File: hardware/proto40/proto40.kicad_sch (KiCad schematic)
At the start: 0 parts

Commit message: Generate Proto40 schematic; add generator, project library and CI checks
- hardware/gen: KiCad 10 schematic generator (library import with extends
  flattening, label/power connections on pin ends, multi-instance
  hierarchical sheets, per-instance references, deterministic UUIDs)
- hardware/lib: VDD5 power symbol, TMUX1308 (4051-compatible pinout,
  flagged for datasheet verification)
- hardware/proto40: root, power (USB-C, LM66100, VDD5 shunt clamp,
  3.3 V), MCU (STM32C071, SWD, UART, UI), control (level shifting, STIM
  driver, ADC taps), 2 x side (DIN 41612 C 2x32, 6 groups, 2nd-stage
  mux, 595, bias driver, ID bus), 12 x group8 (channel cells, mux, 165)
- ERC: 0 violations at all severities; netlist design-intent audit passes
- CI: global lib tables, regeneration diff check, Proto40 audit,
  CI_STAGE=schematic skips DRC until layout
- Decision D13 scoped to the ADP-0001 harness only; F9 updated (external
  clamps omitted on Proto40)

Co-Authored-By: Claude Opus 5.5 <noreply@anthropic.com>
Claude-Session: https://claude.ai/code/session_01UG7pR5ZtgvoVGRWFojzQKf
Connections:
- no-connect marks 0 -> 1
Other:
- added sheet Control (control.kicad_sch)
- added sheet MCU (mcu.kicad_sch)
- added sheet Power (power.kicad_sch)
- added sheet SideA (side.kicad_sch)
- added sheet SideB (side.kicad_sch)
- note added: "Proto40: STM32C071 controller + 2 × (40 fixture nodes + shell + internal test nodes). Generated by hardware/gen/proto40.py. See docs/design-review-and-kicad-plan.md."
- title: ${BOARD_NAME} -> Cable Tester Proto40

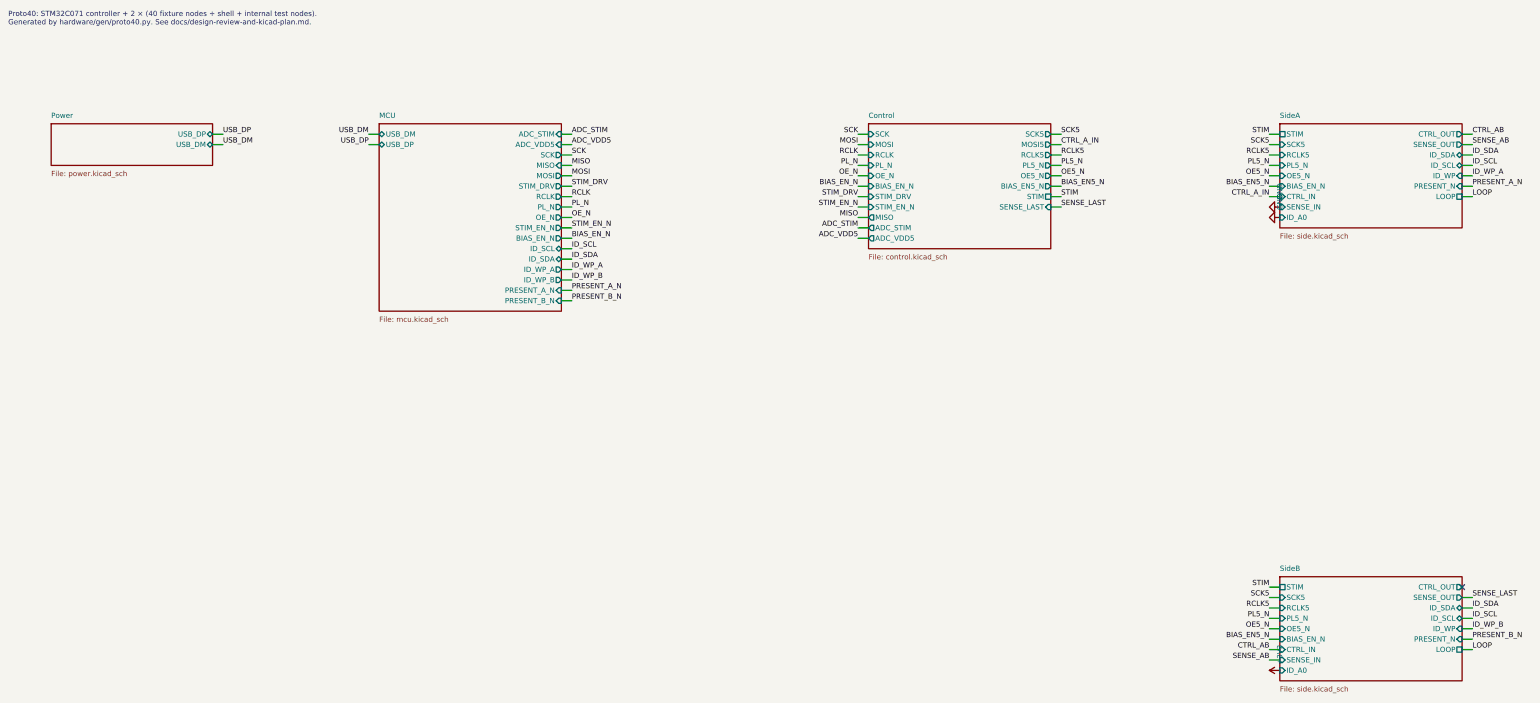
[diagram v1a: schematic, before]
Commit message: Redraw Proto40 schematic with wired functional blocks
Review feedback: text overlapped components and parts were isolated
islands joined only by labels, so connectivity was hard to follow.

- Generator: polyline wires, automatic junctions, text placement from
  the real symbol body graphics, KiCad field-angle handling for rotated
  symbols, power symbols oriented normally on horizontal pins
- Sheets redrawn left-to-right with wired blocks: channel cells, BIAS
  rail, decoupling on IC power pins, pull-ups on their lines, control
  ladder across the six groups, visible 165 chain, wired root hierarchy
  (MCU -> Control -> both sides) and cross-side LOOP
- layoutcheck.py: rejects text/text, text/body, text/wire overlaps and
  wires through bodies; CI runs the generator with --strict
- check_proto40.py: finds parts by sheet path and follows pins, so it no
  longer depends on net names or reference numbering

ERC 0 violations, design-intent audit PASS, layout issues 0.

Co-Authored-By: Claude Opus 5.5 <noreply@anthropic.com>
Claude-Session: https://claude.ai/code/session_01UG7pR5ZtgvoVGRWFojzQKf
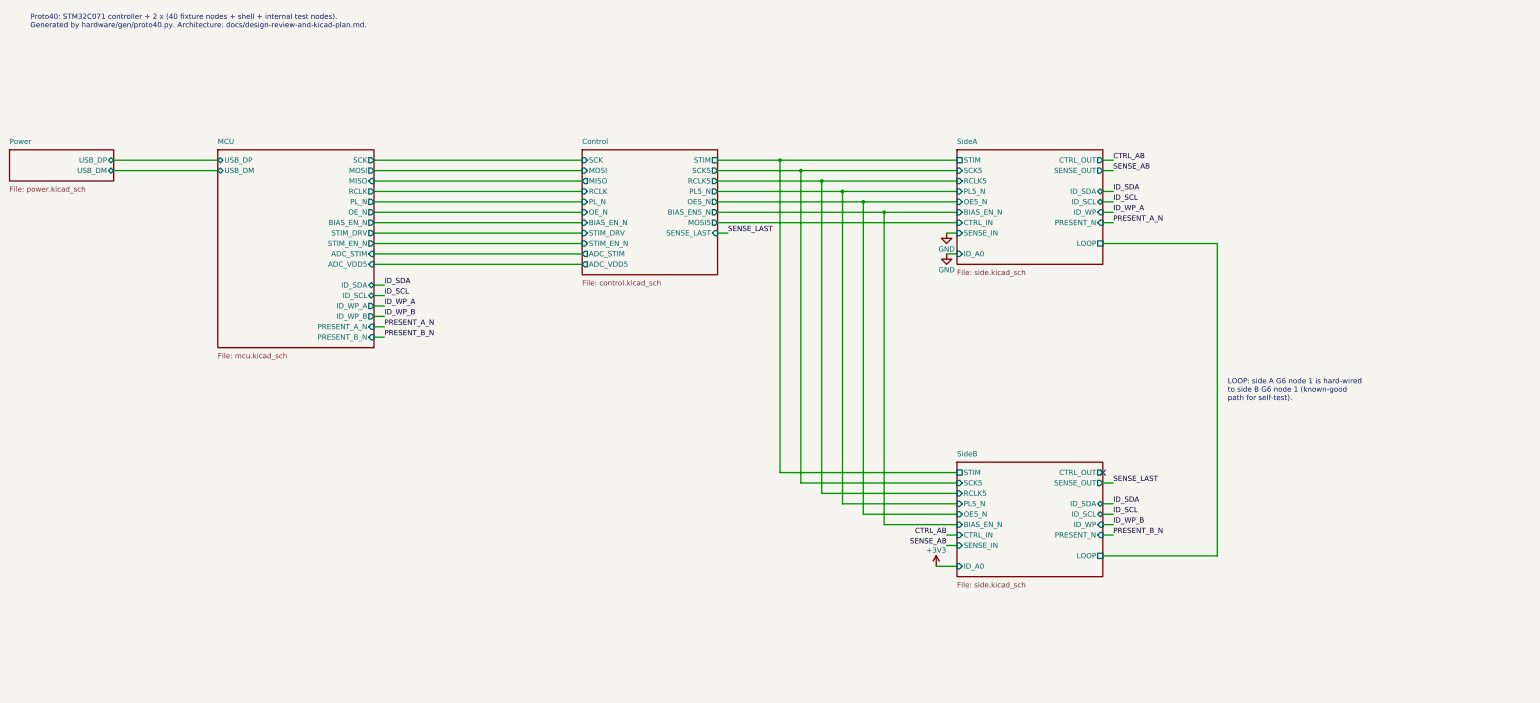
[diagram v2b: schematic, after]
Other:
- note added: "LOOP: side A G6 node 1 is hard-wired to side B G6 node 1 (known-good path for self-test)."
- note added: "Proto40: STM32C071 controller + 2 x (40 fixture nodes + shell + internal test nodes). Generated by hardware/gen/proto40.py. Architecture: docs/design-review-and-kicad-plan.md."
- note removed: "Proto40: STM32C071 controller + 2 × (40 fixture nodes + shell + internal test nodes). Generated by hardware/gen/proto40.py. See docs/design-review-and-kicad-plan.md."
